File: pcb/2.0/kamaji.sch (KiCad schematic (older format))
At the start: 27 parts, among them J1 RJ10, J2 RJ10, J3 RJ10, J4 RJ10, Q1 IRF540N, SW1 CTRL1, SW2 CTRL2, SW3 CTRL3, Y1 Crystal

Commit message: minor changes to the 2.0 schematic
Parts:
- added C?: 1uF, Capacitors_THT:C_Disc_D3.8mm_W2.6mm_P2.50mm, symbol C
- added R?: 10K, Resistors_THT:R_Axial_DIN0207_L6.3mm_D2.5mm_P10.16mm_Horizontal, symbol R
- added R? (x2): 22R, symbol R
- added U?: ATmega32U4, symbol ATmega32U4
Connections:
- net labels added: USB_D+, USB_D-
- wire segments 42 -> 52
- no-connect marks 10 -> 8
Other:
- note added: "Crystal oscillator"
- note added: "TODO: Find out whether\nan inductor is needed on VBUS"
- note removed: "External oscillator"
- moved on the sheet: C3, R5, RV2

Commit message: a few connections on the 2.0 PCB schematic
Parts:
- removed CP1: 1uF, Capacitors_THT:CP_Radial_D4.0mm_P1.50mm, symbol CP
- removed LS1: Speaker, kamaji:AL-30P, symbol Speaker
- removed R3: 100R, Resistors_THT:R_Axial_DIN0207_L6.3mm_D2.5mm_P10.16mm_Horizontal, symbol R
- removed RV1: POT, Potentiometers:Potentiometer_Triwood_RM-065, symbol POT
- added J5: RJ10, kamaji:RJ10, symbol RJ10
- added R11: 220R, Resistors_THT:R_Axial_DIN0207_L6.3mm_D2.5mm_P10.16mm_Horizontal, symbol R
- DS1: symbol LCD-016N002L -> LCD-016N002L-RESCUE-kamaji
- Q1: symbol IRF540N -> IRF540N-RESCUE-kamaji
- gave numbers to parts that had none: 5
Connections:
- net labels added: PBTN5, PLED5
- wire segments 52 -> 81
- no-connect marks 8 -> 7
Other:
- note added: "TODO: ICSP"
- note added: "TODO: Sound circuit"
- note added: "TODO: Wire LEDs"
- note added: "USB out (lamp)"
- note removed: "Buzzer"
- note removed: "USB out"
- moved on the sheet: J1, J2, J3, J4, R6, R7, R8, R9

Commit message: PCB 1.0 wiring
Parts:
- added C? (x2): 0.1uF, Capacitors_THT:C_Disc_D3.8mm_W2.6mm_P2.50mm, symbol C
- added F?: Fuse, symbol Fuse
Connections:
- net SND is gone; now on net SCK: U1.9 ((SCLK/PCINT1)PB1)
- net CBTN1: now also U1.30 ((ADC13/OC1B/OC4B/PCINT13)PB6); no longer U1.22 ((XCK1/~CTS~)PD5)
- net CBTN2: now also U1.31 ((OC3A/~OC4A~)PC6); no longer U1.26 ((T1/~OC4D~/ADC9)PD6)
- net CBTN3: now also U1.32 ((ICP3/CLK0/OC4A)PC7); no longer U1.27 ((T0/OC4D/ADC10)PD7)
- net GND: now also C?.1, C?.1
- net MISO: now also U1.11 ((PDO/MISO/PCINT3)PB3)
- net MOSI: now also U1.10 ((PDI/MOSI/PCINT2)PB2)
- net PBTN2: now also U1.20 ((RXD/INT2)PD2); no longer U1.19 ((SDA/INT1)PD1)
- net PBTN3: now also U1.25 ((ICP2/ADC8)PD4); no longer U1.20 ((RXD/INT2)PD2)
- net PBTN4: now also U1.26 ((T1/~OC4D~/ADC9)PD6); no longer U1.21 ((TXD/INT3)PD3)
- net PBTN5: now also U1.28 ((ADC11/PCINT4)PB4); no longer U1.25 ((ICP2/ADC8)PD4)
- net PLED1: now also U1.19 ((SDA/INT1)PD1)
- net PLED2: now also U1.21 ((TXD/INT3)PD3)
- net PLED3: now also U1.22 ((XCK1/~CTS~)PD5)
- net PLED4: now also U1.27 ((T0/OC4D/ADC10)PD7)
- net PLED5: now also U1.29 ((ADC12/OC1A/~OC4B~/PCINT12)PB5)
- net VCC: now also C?.2, C?.2, F?.1; no longer USB_IN1.1 (VBUS)
- new net: F?.2, USB_IN1.1 (VBUS)
- no-connect marks 7 -> 11
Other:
- note added: "TODO: Check whether\nreset is active HIGH"
- note removed: "TODO: Find out whether\nan inductor is needed on VBUS"
- note removed: "TODO: ICSP"
- note removed: "TODO: Wire LEDs"
- moved on the sheet: C1, C3, DS1, R1, R10, R4, R5, RV2, U1

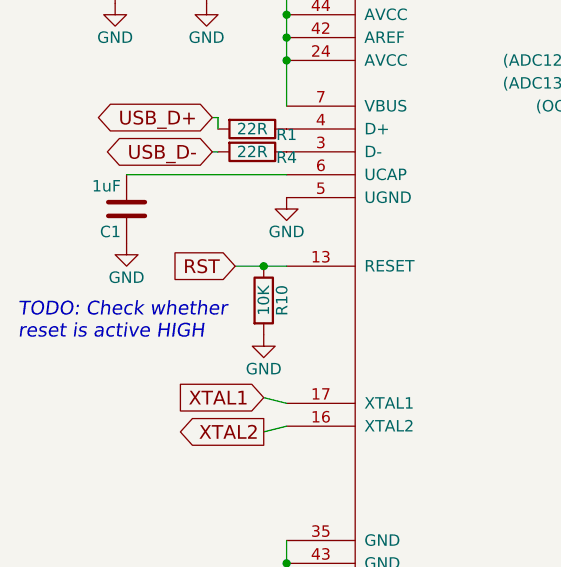
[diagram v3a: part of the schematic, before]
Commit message: pull reset up since it's active-low
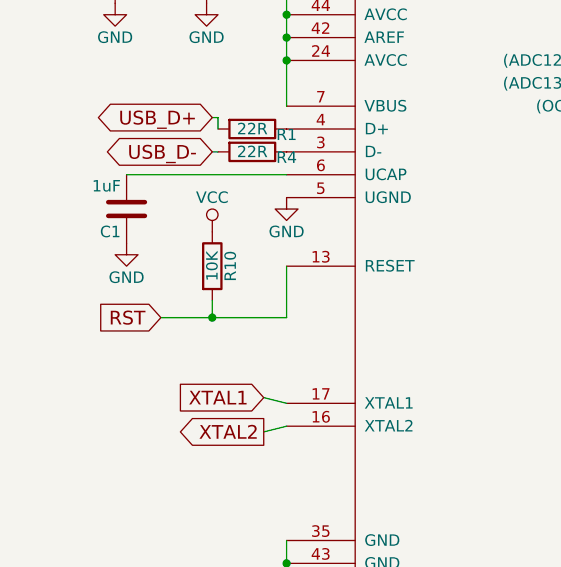
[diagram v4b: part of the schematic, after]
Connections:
- net GND: no longer R10.2
- net RST: now also R10.2; no longer R10.1
- net VCC: now also R10.1
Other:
- note removed: "TODO: Check whether\nreset is active HIGH"
- moved on the sheet: R10
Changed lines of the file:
@@
 L R R10
 U 1 1 59994EA2
-P 1700 2475
-F 0 "R10" V 1780 2475 50  0000 C CNN
-F 1 "10K" V 1700 2475 50  0000 C CNN
-F 2 "Resistors_THT:R_Axial_DIN0207_L6.3mm_D2.5mm_P10.16mm_Horizontal" V 1630 2475 50  0001 C CNN
-F 3 "" H 1700 2475 50  0001 C CNN
-	1    1700 2475
-	1    0    0    -1
-$EndComp
-$Comp
-L GND #PWR3
-U 1 1 5999504B
-P 1700 2625
-F 0 "#PWR3" H 1700 2375 50  0001 C CNN
-F 1 "GND" H 1700 2475 50  0000 C CNN
-F 2 "" H 1700 2625 50  0001 C CNN
-F 3 "" H 1700 2625 50  0001 C CNN
-	1    1700 2625
-	1    0    0    -1
-$EndComp
-Text GLabel 1575 2325 0    60   Input ~ 0
+P 1475 2325
+F 0 "R10" V 1555 2325 50  0000 C CNN
+F 1 "10K" V 1475 2325 50  0000 C CNN
+F 2 "Resistors_THT:R_Axial_DIN0207_L6.3mm_D2.5mm_P10.16mm_Horizontal" V 1405 2325 50  0001 C CNN
+F 3 "" H 1475 2325 50  0001 C CNN
+	1    1475 2325
+	1    0    0    -1
+$EndComp
+Text GLabel 1250 2550 0    60   Input ~ 0
 RST
 $Comp
@@
 Text GLabel 4300 825  1    60   Input ~ 0
 SCK
-Text Notes 625  2650 0    60   Italic 0
-TODO: Check whether\nreset is active HIGH
 $Comp
 L Fuse F?
@@
 Connection ~ 1800 3625
 Wire Wire Line
-	1575 2325 1800 2325
-Connection ~ 1700 2325
-Wire Wire Line
 	7950 5050 8050 5025
 Wire Wire Line
@@
 	1    0    0    -1
 $EndComp
+$Comp
+L VCC #PWR?
+U 1 1 59DBCA86
+P 1475 2175
+F 0 "#PWR?" H 1475 2025 50  0001 C CNN
+F 1 "VCC" H 1475 2325 50  0000 C CNN
+F 2 "" H 1475 2175 50  0001 C CNN
+F 3 "" H 1475 2175 50  0001 C CNN
+	1    1475 2175
+	1    0    0    -1
+$EndComp
+Wire Wire Line
+	1250 2550 1800 2550
+Wire Wire Line
+	1800 2550 1800 2325
+Wire Wire Line
+	1475 2475 1475 2550
+Connection ~ 1475 2550
 $EndSCHEMATC

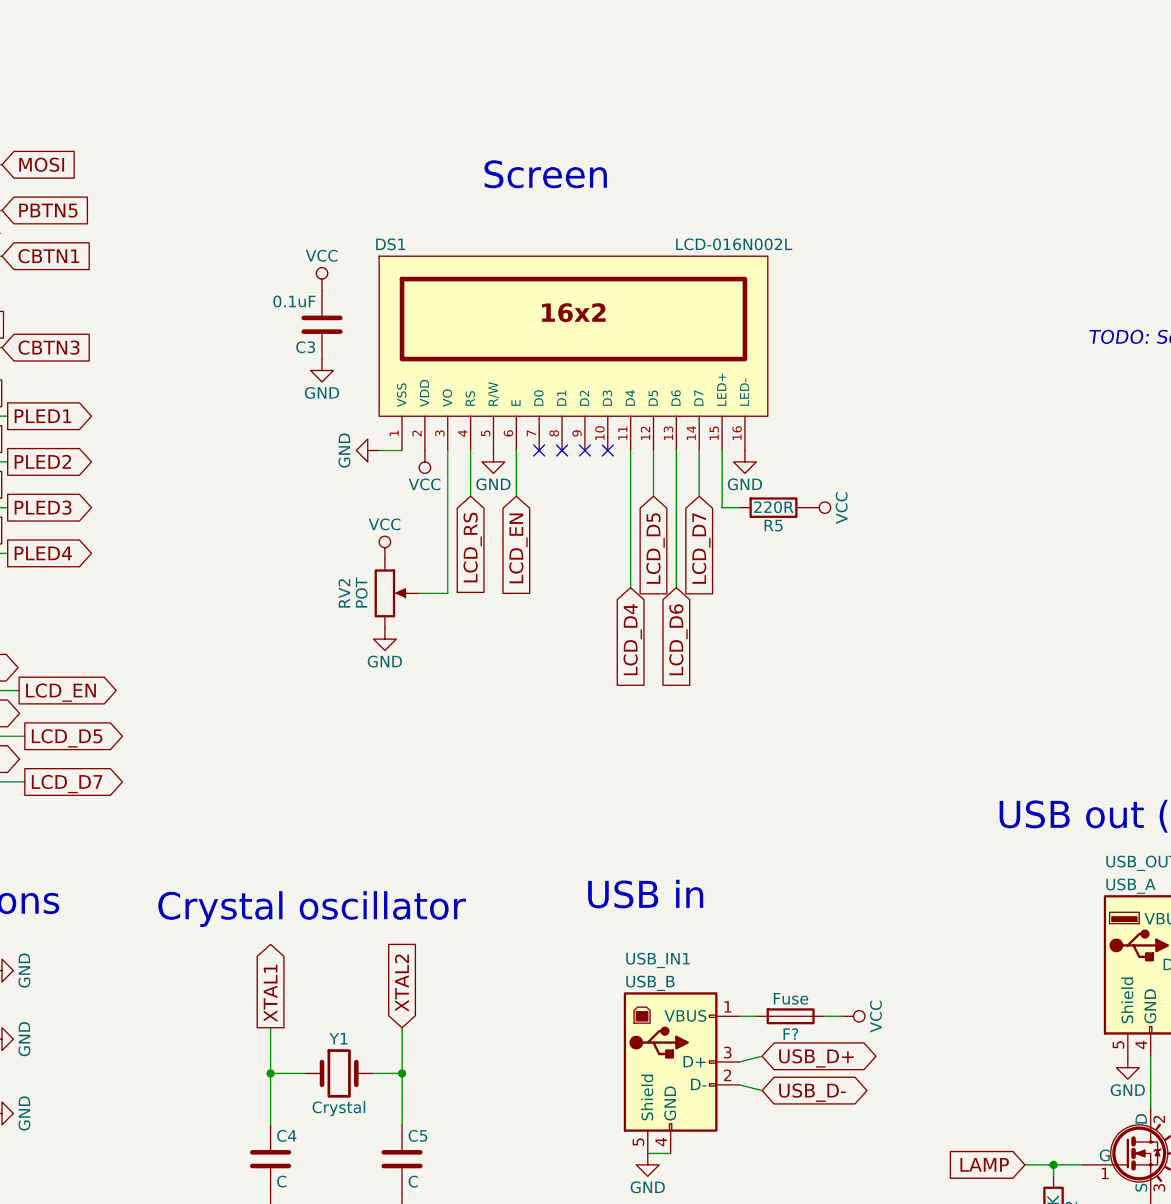
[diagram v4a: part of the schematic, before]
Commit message: add jumper on power, comments
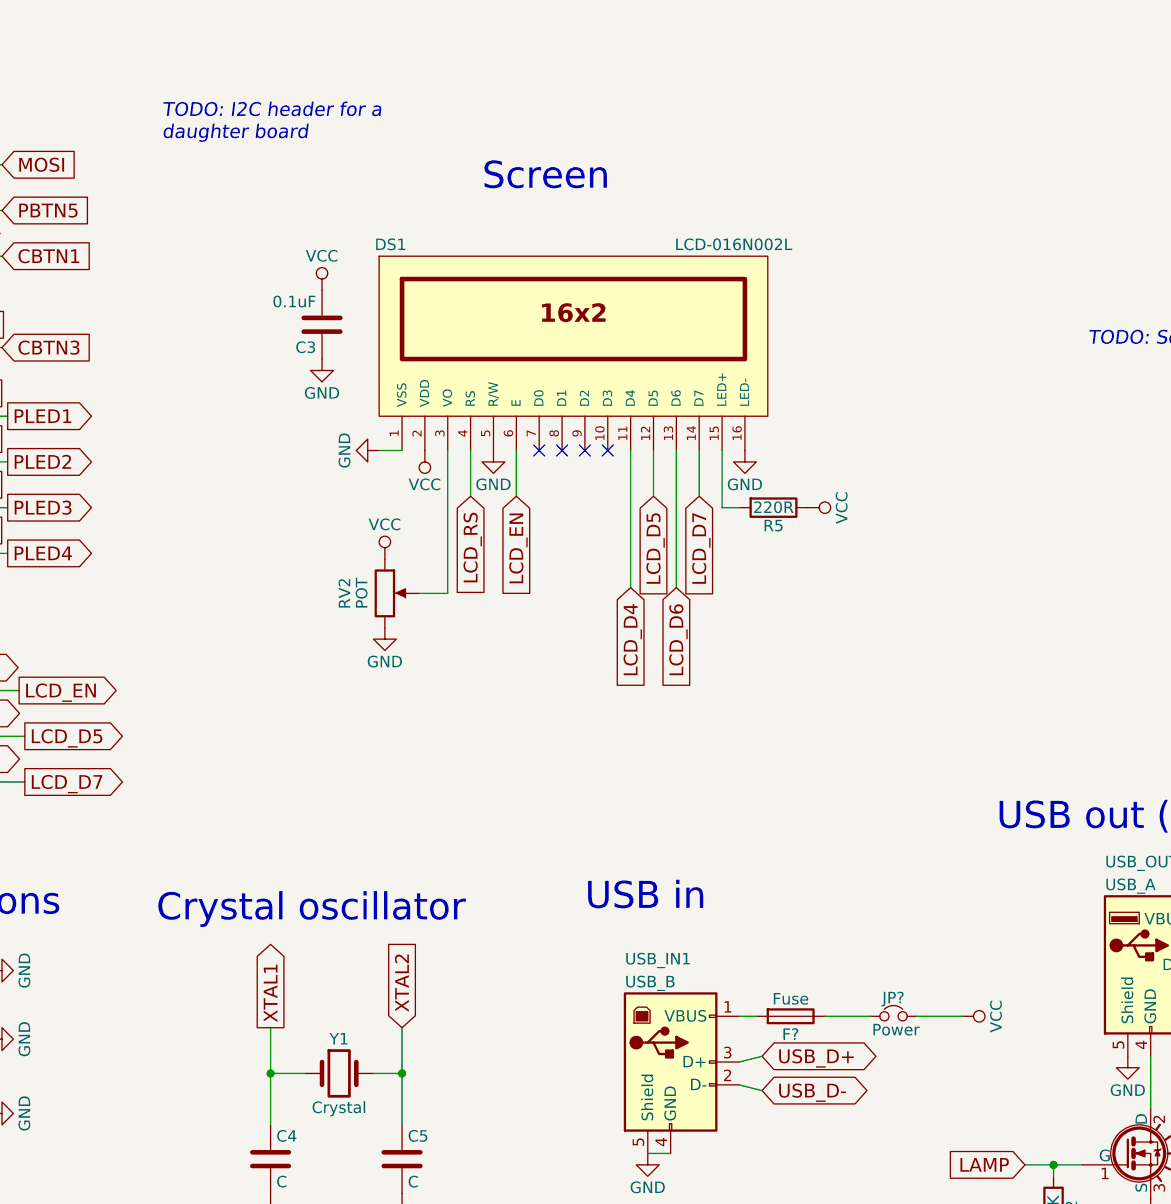
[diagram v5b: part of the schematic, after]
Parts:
- added JP?: Power, symbol Jumper_NC_Small
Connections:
- net VCC: now also JP?.2; no longer F?.1
- new net: F?.1, JP?.1
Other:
- note added: "TODO: I2C header for a\ndaughter board"
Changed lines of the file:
@@
 L VCC #PWR31
 U 1 1 596B3963
-P 8400 4850
-F 0 "#PWR31" H 8400 4700 50  0001 C CNN
-F 1 "VCC" H 8400 5000 50  0000 C CNN
-F 2 "" H 8400 4850 50  0001 C CNN
-F 3 "" H 8400 4850 50  0001 C CNN
-	1    8400 4850
+P 8925 4850
+F 0 "#PWR31" H 8925 4700 50  0001 C CNN
+F 1 "VCC" H 8925 5000 50  0000 C CNN
+F 2 "" H 8925 4850 50  0001 C CNN
+F 3 "" H 8925 4850 50  0001 C CNN
+	1    8925 4850
 	0    1    1    0
 $EndComp
@@
 Wire Wire Line
 	7950 4850 8025 4850
-Wire Wire Line
-	8325 4850 8400 4850
 Text GLabel 4750 2425 2    60   Output ~ 0
 PLED2
@@
 	1475 2475 1475 2550
 Connection ~ 1475 2550
+Text Notes 5425 1025 0    60   Italic 0
+TODO: I2C header for a\ndaughter board
+$Comp
+L Jumper_NC_Small JP?
+U 1 1 59DBDD2F
+P 8625 4850
+F 0 "JP?" H 8625 4930 50  0000 C CNN
+F 1 "Power" H 8635 4790 50  0000 C CNN
+F 2 "" H 8625 4850 50  0001 C CNN
+F 3 "" H 8625 4850 50  0001 C CNN
+	1    8625 4850
+	1    0    0    -1
+$EndComp
+Wire Wire Line
+	8325 4850 8525 4850
+Wire Wire Line
+	8725 4850 8925 4850
 $EndSCHEMATC

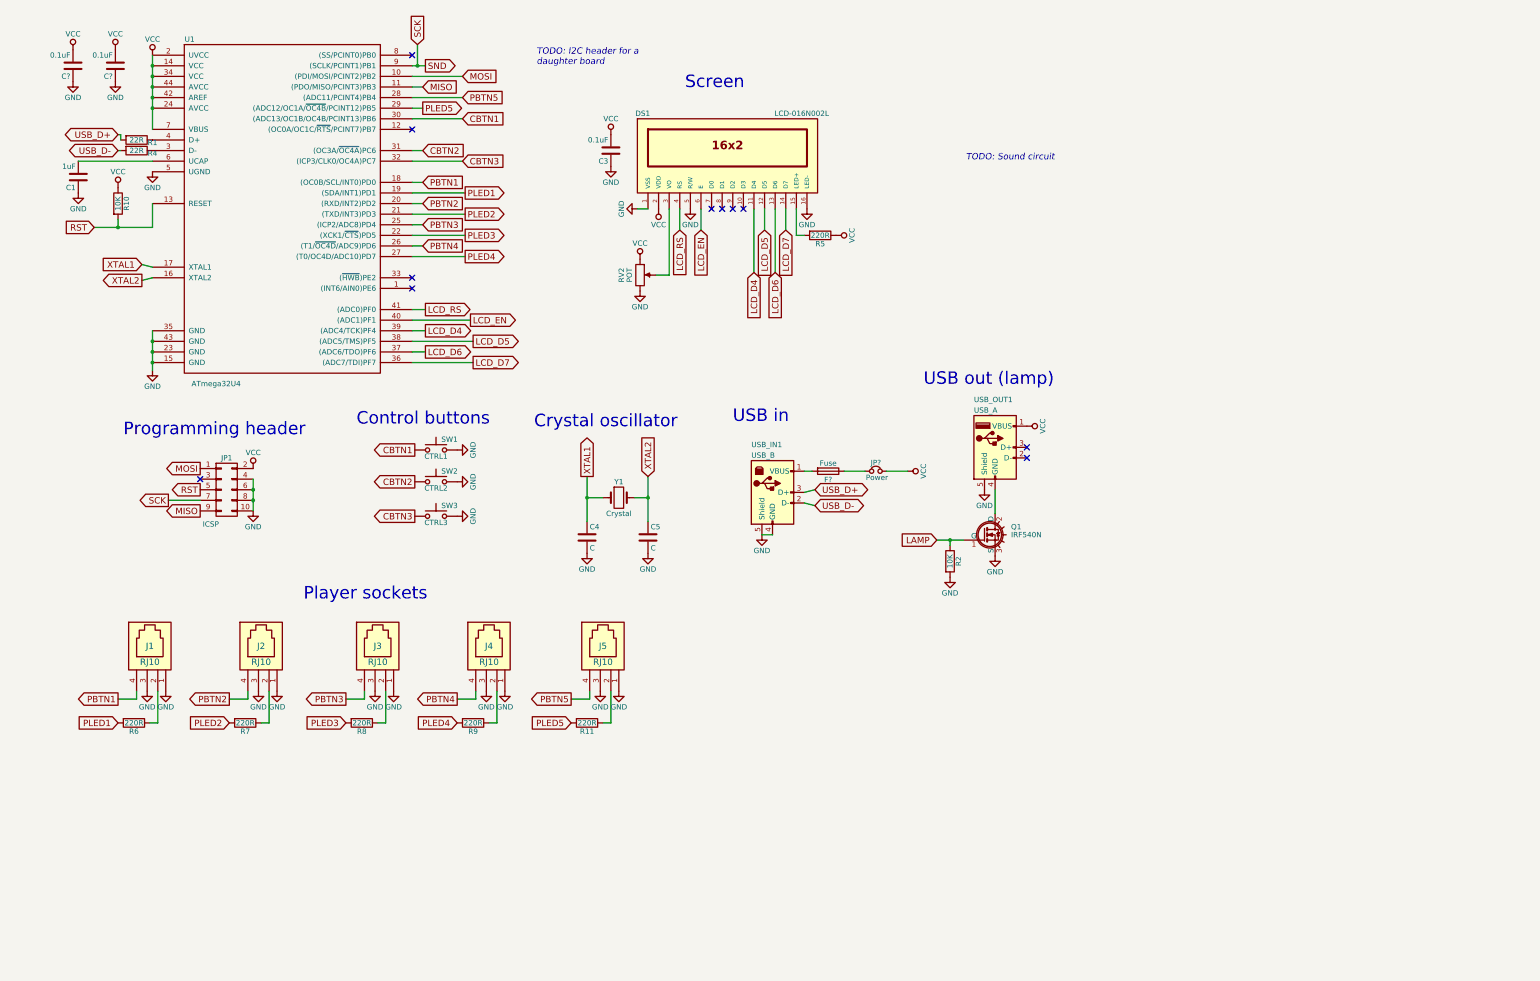
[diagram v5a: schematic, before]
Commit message: add a daughter board connector
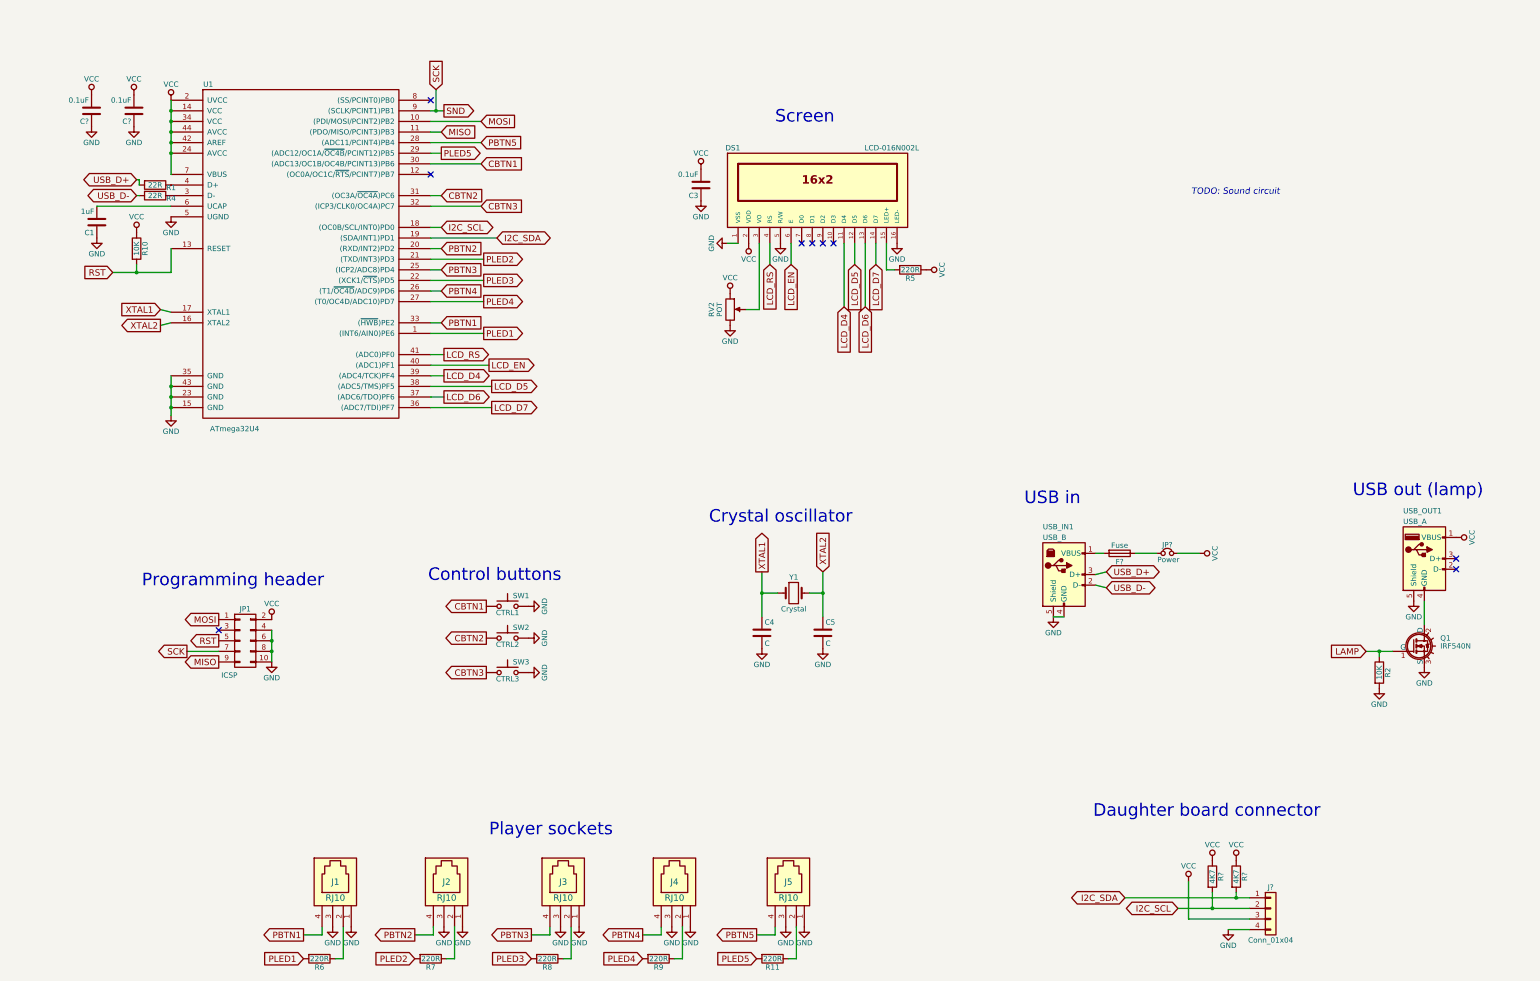
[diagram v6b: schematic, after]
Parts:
- added J?: Conn_01x04, symbol Conn_01x04
- added R? (x2): 4K7, symbol R
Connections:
- net GND: now also J?.4 (Pin_4)
- net PBTN1: now also U1.33 ((~HWB~)PE2); no longer U1.18 ((OC0B/SCL/INT0)PD0)
- net PLED1: now also U1.1 ((INT6/AIN0)PE6); no longer U1.19 ((SDA/INT1)PD1)
- net VCC: now also J?.3 (Pin_3), R?.1, R?.1
- new net I2C_SCL: J?.2 (Pin_2), R?.2, U1.18 ((OC0B/SCL/INT0)PD0)
- new net I2C_SDA: J?.1 (Pin_1), R?.2, U1.19 ((SDA/INT1)PD1)
- no-connect marks 11 -> 9
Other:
- note added: "Daughter board connector"
- note removed: "TODO: I2C header for a\ndaughter board"
- moved on the sheet: C1, C3, C4, C5, C?, DS1, F?, J1, J2, J3, J4, J5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
